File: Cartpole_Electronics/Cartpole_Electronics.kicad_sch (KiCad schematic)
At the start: 8 parts, among them M1 Motor_DC, M2 Motor_DC, M3 Motor_DC, M4 Motor_DC, U1 L298N, U2 L298N, U3 MPU-6050

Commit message: Added ground bus
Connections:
- net GND: now reaches A1.29 (GND)
- net GND: now also U1.8 (GND), U2.8 (GND), U3.18 (GND)

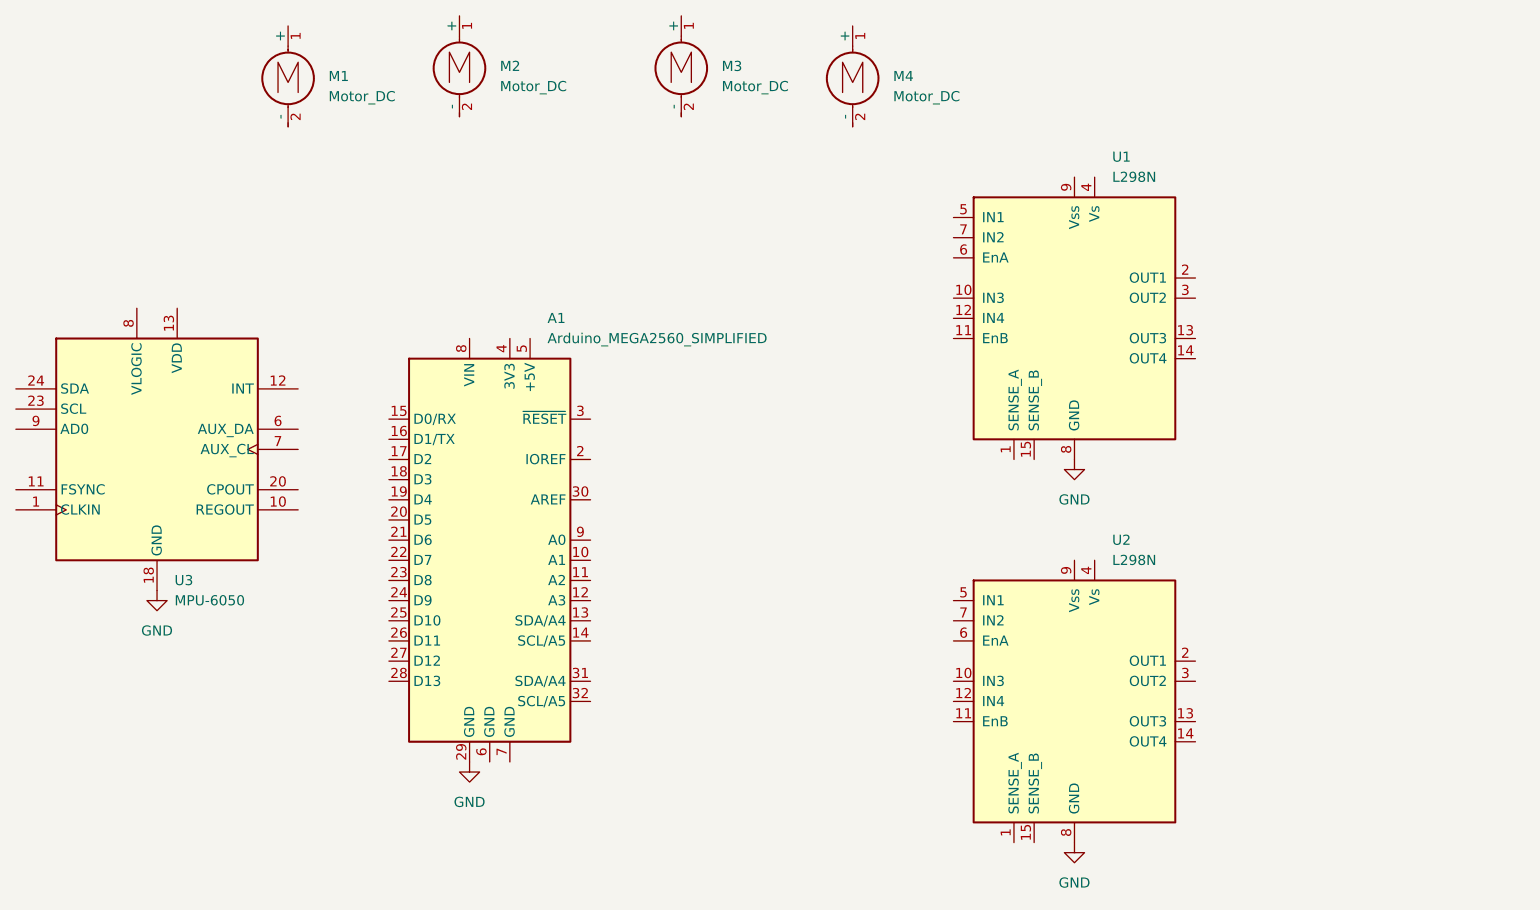
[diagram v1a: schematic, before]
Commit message: Add wiring for schematic
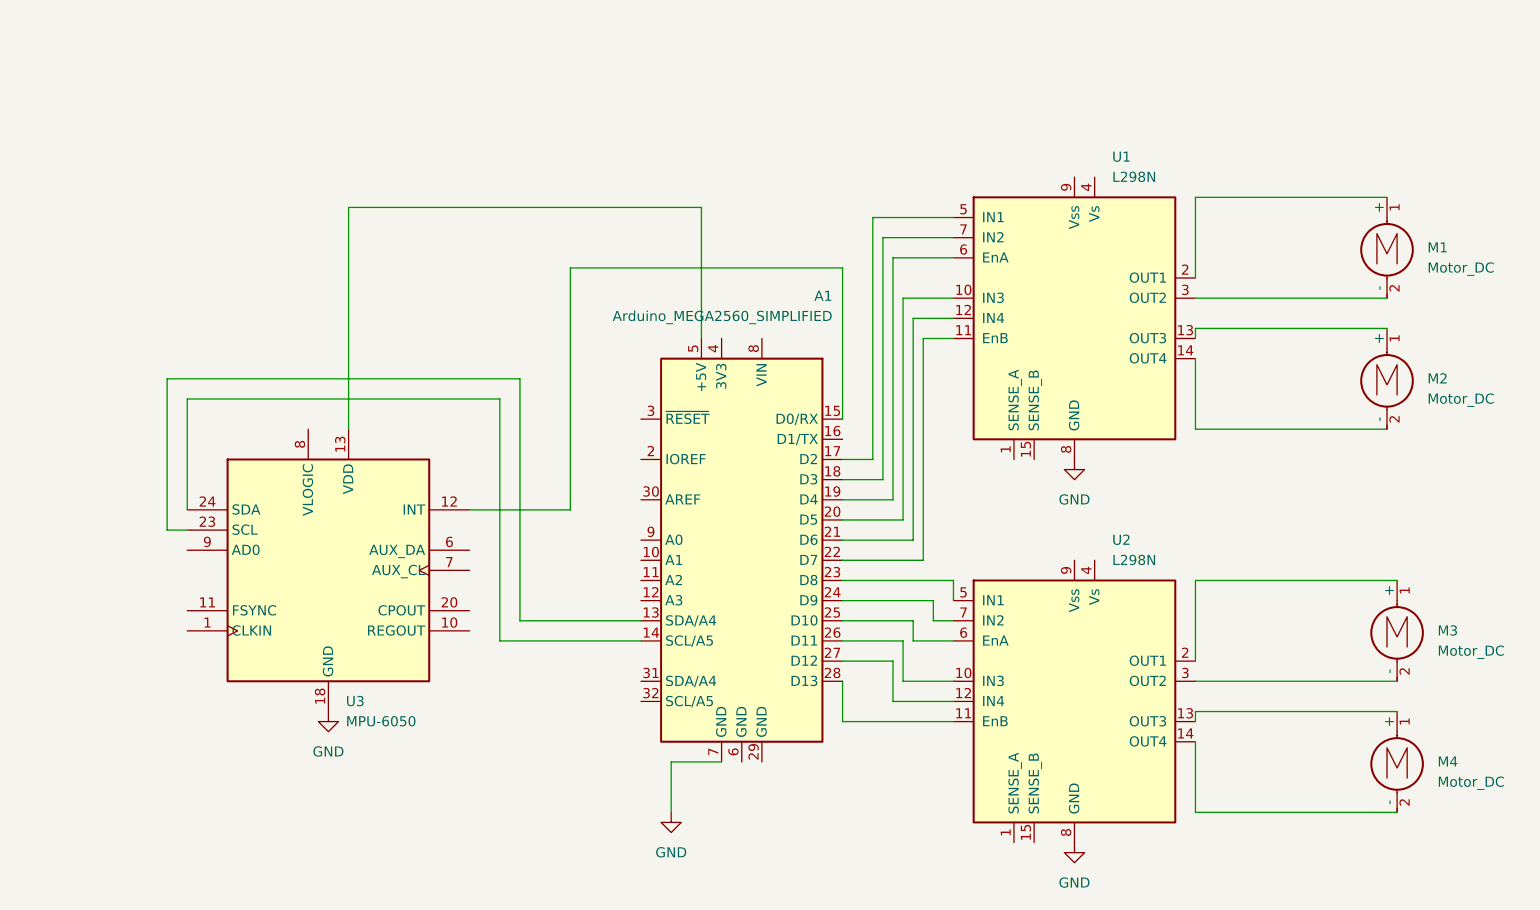
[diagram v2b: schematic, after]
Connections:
- net GND: now also A1.7 (GND); no longer A1.29 (GND)
- net at A1.13 (SDA/A4): now also U3.23 (SCL)
- net at A1.14 (SCL/A5): now also U3.24 (SDA)
- net at A1.15 (D0/RX): now also U3.12 (INT)
- net at A1.17 (D2): now also U1.5 (IN1)
- net at A1.18 (D3): now also U1.7 (IN2)
- net at A1.19 (D4): now also U1.6 (EnA)
- net at A1.20 (D5): now also U1.10 (IN3)
- net at A1.21 (D6): now also U1.12 (IN4)
- net at A1.22 (D7): now also U1.11 (EnB)
- net at A1.23 (D8): now also U2.5 (IN1)
- net at A1.24 (D9): now also U2.7 (IN2)
- net at A1.25 (D10): now also U2.6 (EnA)
- net at A1.26 (D11): now also U2.10 (IN3)
- net at A1.27 (D12): now also U2.12 (IN4)
- net at A1.28 (D13): now also U2.11 (EnB)
- net at A1.5 (+5V): now also U3.13 (VDD)
- net at M2.1 (+): now also U1.13 (OUT3)
- net at M2.2 (-): now also U1.14 (OUT4)
- net at M3.1 (+): now also U2.2 (OUT1)
- net at M3.2 (-): now also U2.3 (OUT2)
- net at U2.13 (OUT3): now also M4.1 (+)
- net at U2.14 (OUT4): now also M4.2 (-)
- net at M1.1 (+): now also U1.2 (OUT1)
- net at M1.2 (-): now also U1.3 (OUT2)
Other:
- moved on the sheet: A1, M1, M2, M3, M4, U3

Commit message: Complete schematic
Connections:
- net at A1.5 (+5V): no longer U3.13 (VDD)
- net +12V: now reaches U2.4 (Vs)
- net +12V: now also U1.4 (Vs)
- net +5V: now reaches U2.9 (Vss)
- net +5V: now also U1.9 (Vss), U3.13 (VDD)
